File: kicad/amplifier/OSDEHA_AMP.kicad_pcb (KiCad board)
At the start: 2 copper layers, 190.1 x 71.6 mm, 85 parts, among them J1 INPUT, J2 HEATERS DC, J3 PSU HV, J4 OUTPUT, J5 DHT FIL, Q1 DN2540, Q10 DN2540, Q2 DN2540, Q3 STF3LN80K5, Q4 STF3LN80K5, Q5 AOT1N60, Q6 IXTP3N100D2, Q7 AOT1N60, Q8 IXTP3N100D2, Q9 DN2540, SW1 SW_DPDT_x2, U1 6E5P, U2 6E5P, U3 801A, U4 801A

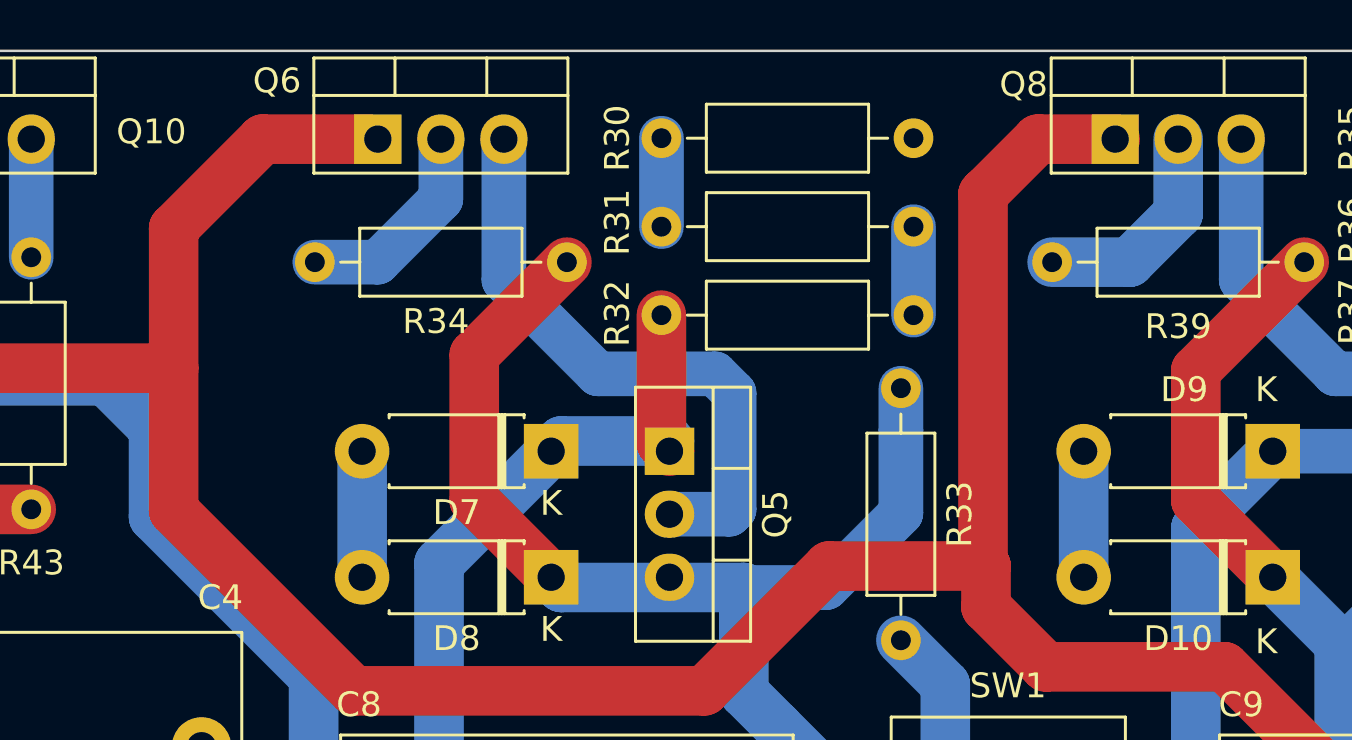
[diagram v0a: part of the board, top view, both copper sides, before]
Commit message: fixed pinout of Q6 and Q8 on PCB
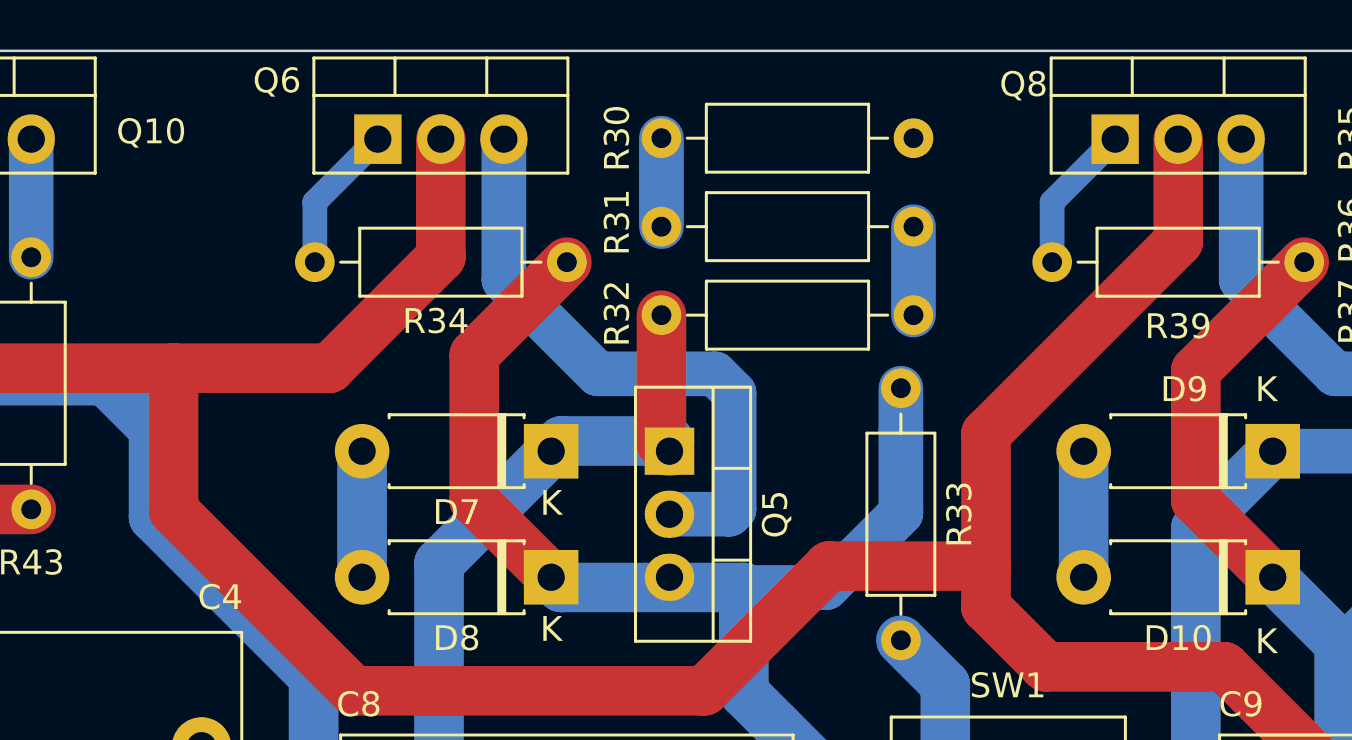
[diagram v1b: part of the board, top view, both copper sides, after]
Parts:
- R15, R20: value 25k -> 18.7k
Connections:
- Q6 pad 1: /B+ -> Net-(Q6-G)
- Q6 pad 2: Net-(Q6-G) -> /B+
- Q8 pad 1: /B+ -> Net-(Q8-G)
- Q8 pad 2: Net-(Q8-G) -> /B+
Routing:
- net Net-(Q8-G): track 9.02 -> 6.01 mm
- net Net-(Q6-G): track 8.55 -> 6.01 mm
- net /B+: track 256.2 -> 257.9 mm
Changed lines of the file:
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@@
 			)
 		)
+		(property ki_fp_filters "TO?220*")
 		(sheetname "Dual_Gyrator")
 		(sheetfile "Gyrator.kicad_sch")
@@
 			(layers "*.Cu" "*.Mask")
 			(remove_unused_layers no)
-			(net 17 "/B+")
-			(pinfunction "D")
-			(pintype "passive")
+			(net 27 "Net-(Q8-G)")
+			(pinfunction "G")
+			(pintype "input")
 		)
 		(pad "2" thru_hole oval
@@
 			(layers "*.Cu" "*.Mask")
 			(remove_unused_layers no)
-			(net 27 "Net-(Q8-G)")
-			(pinfunction "G")
-			(pintype "input")
+			(net 17 "/B+")
+			(pinfunction "D")
+			(pintype "passive")
 		)
 		(pad "3" thru_hole oval
@@
 			)
 		)
-		(property "Value" "25k"
+		(property "Value" "18.7k"
 			(at 5.08 2.37 90)
 			(layer "F.Fab")
@@
 			)
 		)
-		(property "MPN" "CMF5525K000"
+		(property "MPN" "CMF5520K000"
 			(at 0 0 0)
 			(layer "F.Fab")
@@
 			)
 		)
+		(property ki_fp_filters "TO?220*")
 		(sheetname "Dual_Gyrator")
 		(sheetfile "Gyrator.kicad_sch")
@@
 			(layers "*.Cu" "*.Mask")
 			(remove_unused_layers no)
-			(net 17 "/B+")
-			(pinfunction "D")
-			(pintype "passive")
+			(net 25 "Net-(Q6-G)")
+			(pinfunction "G")
+			(pintype "input")
 		)
 		(pad "2" thru_hole oval
@@
 			(layers "*.Cu" "*.Mask")
 			(remove_unused_layers no)
-			(net 25 "Net-(Q6-G)")
-			(pinfunction "G")
-			(pintype "input")
+			(net 17 "/B+")
+			(pinfunction "D")
+			(pintype "passive")
 		)
 		(pad "3" thru_hole oval
@@
 			(pintype "passive")
 		)
-		(model "${KICAD6_3DMODEL_DIR}/Package_TO_SOT_THT.3dshapes/TO-220-3_Vertical.wrl"
+		(model "${KICAD8_3DMODEL_DIR}/Package_TO_SOT_THT.3dshapes/TO-220-3_Vertical.wrl"
 			(offset
 				(xyz 0 0 0)
@@
 			)
 		)
-		(property "Value" "25k"
+		(property "Value" "18.7k"
 			(at 5.08 2.37 90)
 			(layer "F.Fab")
@@
 			)
 		)
-		(property "MPN" "CMF5525K000"
+		(property "MPN" "CMF5520K000"
 			(at 0 0 0)
 			(layer "F.Fab")
@@
 	)
 	(segment
-		(start 192.4304 56.7436)
-		(end 196.024 53.15)
+		(start 225.171 65.029)
+		(end 225.171 70.358)
+		(width 2)
+		(layer "F.Cu")
+		(net 17)
+	)
+	(segment
+		(start 198.7176 62.3824)
+		(end 192.4304 62.3824)
 		(width 2)
 		(layer "F.Cu")
@@
 	)
 	(segment
-		(start 196.024 53.15)
-		(end 200.2475 53.15)
-		(width 2)
-		(layer "F.Cu")
-		(net 17)
-	)
-	(segment
-		(start 225.05 70.237)
-		(end 225.171 70.358)
-		(width 2)
-		(layer "F.Cu")
-		(net 17)
-	)
-	(segment
-		(start 225.171 55.245)
-		(end 227.266 53.15)
+		(start 192.4304 62.3824)
+		(end 192.4304 68.1228)
 		(width 2)
 		(layer "F.Cu")
@@
 	)
 	(segment
-		(start 225.05 55.366)
-		(end 225.171 55.245)
+		(start 203.2 53.15)
+		(end 203.2 57.9)
 		(width 2)
 		(layer "F.Cu")
@@
 	)
 	(segment
-		(start 225.05 70.237)
-		(end 225.05 55.366)
+		(start 203.2 57.9)
+		(end 198.7176 62.3824)
 		(width 2)
 		(layer "F.Cu")
@@
 	)
 	(segment
-		(start 227.266 53.15)
-		(end 230.378 53.15)
+		(start 232.918 57.282)
+		(end 225.171 65.029)
 		(width 2)
 		(layer "F.Cu")
@@
 	)
 	(segment
-		(start 225.171 70.358)
-		(end 225.171 72.009)
+		(start 232.918 53.15)
+		(end 232.918 57.282)
 		(width 2)
 		(layer "F.Cu")
@@
 	)
 	(segment
-		(start 192.4304 56.7436)
-		(end 192.4304 68.1228)
+		(start 225.171 70.358)
+		(end 225.171 72.009)
 		(width 2)
 		(layer "F.Cu")
@@
 	)
 	(segment
+		(start 232.918 53.15)
+		(end 233.0055 53.2375)
+		(width 1)
+		(layer "B.Cu")
+		(net 17)
+	)
+	(segment
 		(start 87.5792 55.88)
 		(end 84.7142 53.015)
@@
 	)
 	(segment
-		(start 203.2 55.5625)
-		(end 200.6525 58.11)
-		(width 1.8)
-		(layer "B.Cu")
-		(net 25)
-	)
-	(segment
-		(start 200.6525 58.11)
-		(end 198.12 58.11)
-		(width 1.8)
+		(start 198.12 58.11)
+		(end 198.12 55.69)
+		(width 1)
 		(layer "B.Cu")
 		(net 25)
 	)
 	(segment
-		(start 203.2 53.15)
-		(end 203.2 55.5625)
-		(width 1.8)
+		(start 198.12 55.69)
+		(end 200.66 53.15)
+		(width 1)
 		(layer "B.Cu")
 		(net 25)
@@
 	)
 	(segment
-		(start 230.958 58.11)
-		(end 232.918 56.15)
-		(width 2)
+		(start 227.838 55.69)
+		(end 230.378 53.15)
+		(width 1)
 		(layer "B.Cu")
 		(net 27)
@@
 	(segment
 		(start 227.838 58.11)
-		(end 230.958 58.11)
-		(width 2)
-		(layer "B.Cu")
-		(net 27)
-	)
-	(segment
-		(start 232.918 56.15)
-		(end 232.918 53.15)
-		(width 2)
-		(layer "B.Cu")
-		(net 27)
-	)
-	(segment
-		(start 232.918 53.15)
-		(end 233.0055 53.2375)
+		(end 227.838 55.69)
 		(width 1)
 		(layer "B.Cu")

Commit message: changed R13 and R18 from 1M to 100k in schematic and PCB
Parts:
- R13, R18: value 1M -> 100k
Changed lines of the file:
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@@
 			)
 		)
-		(property "Value" "1M"
+		(property "Value" "100k"
 			(at 5.08 2.37 0)
 			(layer "F.Fab")
@@
 			)
 		)
-		(property "Value" "1M"
+		(property "Value" "100k"
 			(at 5.08 2.37 0)
 			(layer "F.Fab")

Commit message: revise R values in schematic and PCB files. Expand test/design notes.
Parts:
- R30, R31, R32, R35, R36, R37: value 1.5M -> 270k
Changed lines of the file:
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@@
 			)
 		)
-		(property "Value" "1.5M"
+		(property "Value" "270k"
 			(at 5.08 2.37 0)
 			(layer "F.Fab")
@@
 			)
 		)
-		(property "MPN" "CMF551M5000"
+		(property "MPN" "CMF55270K00"
 			(at 0 0 0)
 			(layer "F.Fab")
@@
 			)
 		)
-		(property "Value" "1.5M"
+		(property "Value" "270k"
 			(at 5.08 2.37 0)
 			(layer "F.Fab")
@@
 			)
 		)
-		(property "MPN" "CMF551M5000"
+		(property "MPN" "CMF55270K00"
 			(at 0 0 0)
 			(layer "F.Fab")
@@
 			)
 		)
-		(property "MPN" "CMF551M000"
+		(property "MPN" "CMF55100K00"
 			(at 0 0 0)
 			(layer "F.Fab")
@@
 			)
 		)
-		(property "Value" "1.5M"
+		(property "Value" "270k"
 			(at 5.08 2.37 0)
 			(layer "F.Fab")
@@
 			)
 		)
-		(property "MPN" "CMF551M5000"
+		(property "MPN" "CMF55270K00"
 			(at 0 0 0)
 			(layer "F.Fab")
@@
 			)
 		)
-		(property "Value" "1.5M"
+		(property "Value" "270k"
 			(at 5.08 2.37 0)
 			(layer "F.Fab")
@@
 			)
 		)
-		(property "MPN" "CMF551M5000"
+		(property "MPN" "CMF55270K00"
 			(at 0 0 0)
 			(layer "F.Fab")
@@
 			)
 		)
-		(property "Value" "1.5M"
+		(property "Value" "270k"
 			(at 5.08 2.37 0)
 			(layer "F.Fab")
@@
 			)
 		)
-		(property "MPN" "CMF551M5000"
+		(property "MPN" "CMF55270K00"
 			(at 0 0 0)
 			(layer "F.Fab")
@@
 			)
 		)
-		(property "MPN" "CMF551M0000"
+		(property "MPN" "CMF55100K00"
 			(at 0 0 0)
 			(layer "F.Fab")
@@
 			)
 		)
-		(property "Value" "1.5M"
+		(property "Value" "270k"
 			(at 5.08 2.37 0)
 			(layer "F.Fab")
@@
 			)
 		)
-		(property "MPN" "CMF551M5000"
+		(property "MPN" "CMF55270K00"
 			(at 0 0 0)
 			(layer "F.Fab")

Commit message: notes, design tweaks
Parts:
- R33, R38: footprint Resistor_THT:R_Axial_DIN0207_L6.3mm_D2.5mm_P10.16mm_Horizontal -> Resistor_THT:R_Axial_DIN0516_L15.5mm_D5.0mm_P5.08mm_Vertical
- moved R33 6.99 mm to (220.2, 70.0), turned to 90 degrees
- moved R38 6.76 mm to (251.2, 70.0), turned to 90 degrees
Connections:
- R33 pad 1: /Dual_Gyrator/MU_OUT1 -> /A1
- R33 pad 2: /A1 -> /Dual_Gyrator/MU_OUT1
- R38 pad 1: /Dual_Gyrator/MU_OUT2 -> /A2
- R38 pad 2: /A2 -> /Dual_Gyrator/MU_OUT2
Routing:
- net /A1: track 74.6 -> 79.0 mm
- net /Dual_Gyrator/MU_OUT1: track 53.9 -> 49.6 mm
- net /A2: track 129.1 -> 132.5 mm
- net /Dual_Gyrator/MU_OUT2: track 61.2 -> 58.3 mm
- net /B+: track 257.9 -> 260.2 mm

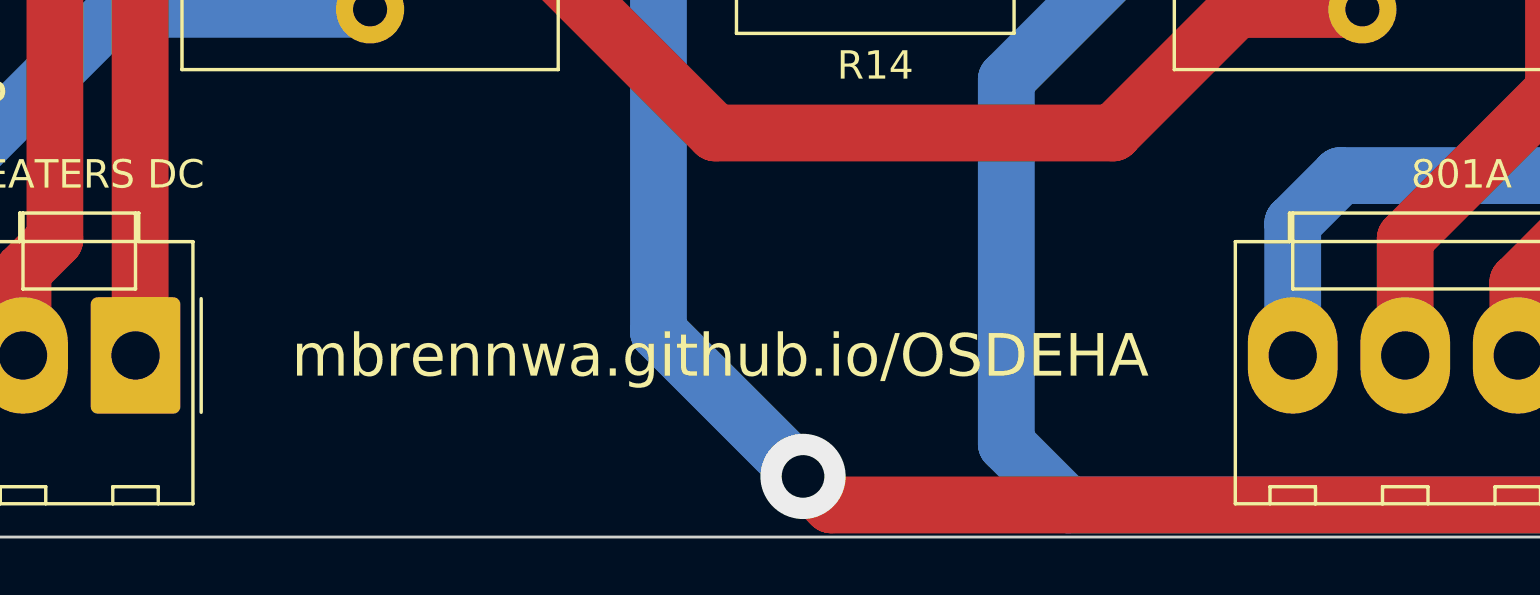
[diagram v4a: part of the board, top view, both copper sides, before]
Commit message: add version info to silk screens (AMP + HV PSU)
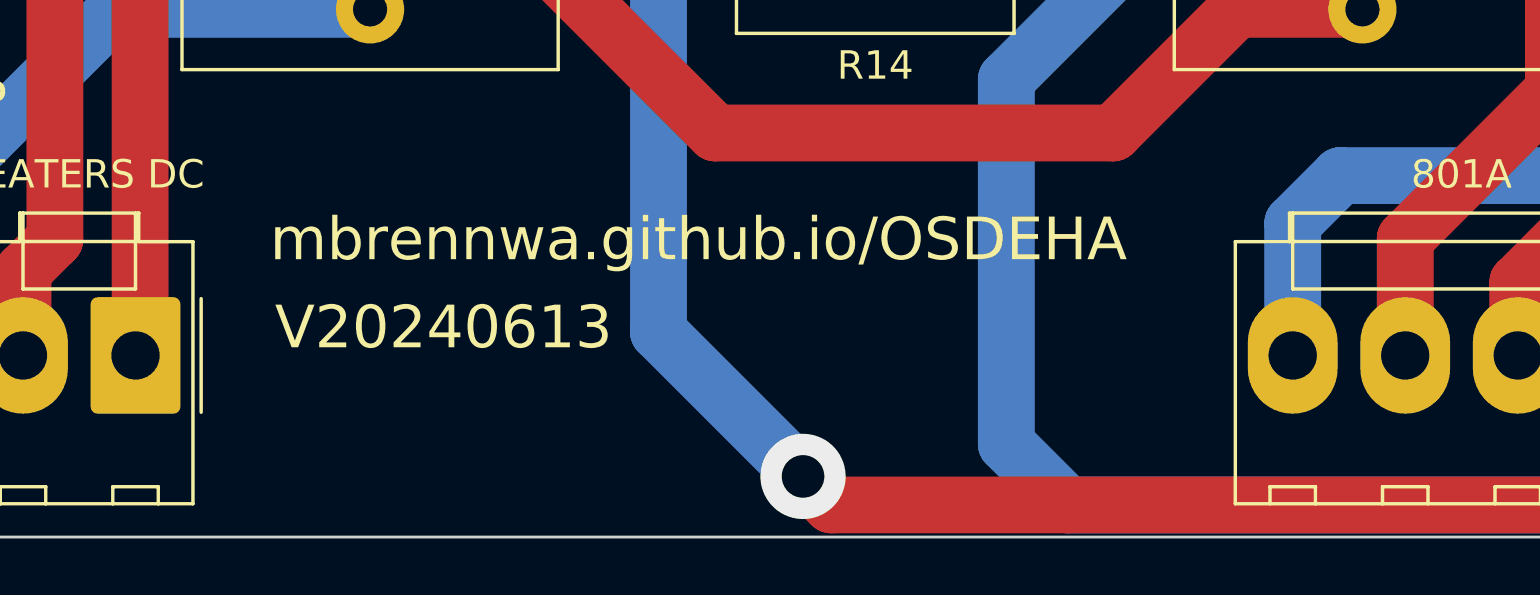
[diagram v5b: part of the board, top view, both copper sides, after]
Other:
- board text added: "V20240613"
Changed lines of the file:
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@@
 		(tags "Resistor Axial_DIN0516 series Axial Vertical pin pitch 5.08mm 2W length 15.5mm diameter 5mm")
 		(property "Reference" "R38"
-			(at 4.6 2.605 270)
+			(at 4.6 2.605 -90)
 			(layer "F.SilkS")
 			(effects
@@
 		)
 		(property "Value" "470"
-			(at 2.54 3.62 270)
+			(at 2.54 3.62 -90)
 			(layer "F.Fab")
 			(hide yes)
@@
 		)
 		(fp_text user "${REFERENCE}"
-			(at 2.54 -3.62 270)
+			(at 2.54 -3.62 -90)
 			(layer "F.Fab")
 			(effects
@@
 		(tags "Resistor Axial_DIN0516 series Axial Vertical pin pitch 5.08mm 2W length 15.5mm diameter 5mm")
 		(property "Reference" "R33"
-			(at 4.59 2.8 270)
+			(at 4.59 2.8 -90)
 			(layer "F.SilkS")
 			(effects
@@
 		)
 		(property "Value" "470"
-			(at 2.54 3.62 270)
+			(at 2.54 3.62 -90)
 			(layer "F.Fab")
 			(hide yes)
@@
 		)
 		(property "MPN" " CPF3470R00"
-			(at 0 0 360)
+			(at 0 0 0)
 			(layer "F.Fab")
 			(hide yes)
@@
 		)
 		(fp_text user "${REFERENCE}"
-			(at 2.54 -3.62 270)
+			(at 2.54 -3.62 -90)
 			(layer "F.Fab")
 			(effects
@@
 		(layer "Edge.Cuts")
 	)
+	(gr_text "V20240613"
+		(at 130 114.725 0)
+		(layer "F.SilkS")
+		(effects
+			(font
+				(size 1.5 1.5)
+				(thickness 0.15)
+			)
+			(justify left bottom)
+		)
+	)
 	(gr_text "mbrennwa.github.io/OSDEHA"
-		(at 145.675 115.725 0)
+		(at 129.825 111.625 0)
 		(layer "F.SilkS")
 		(effects
@@
 				(thickness 0.15)
 			)
-			(justify bottom)
+			(justify left bottom)
 		)
 	)

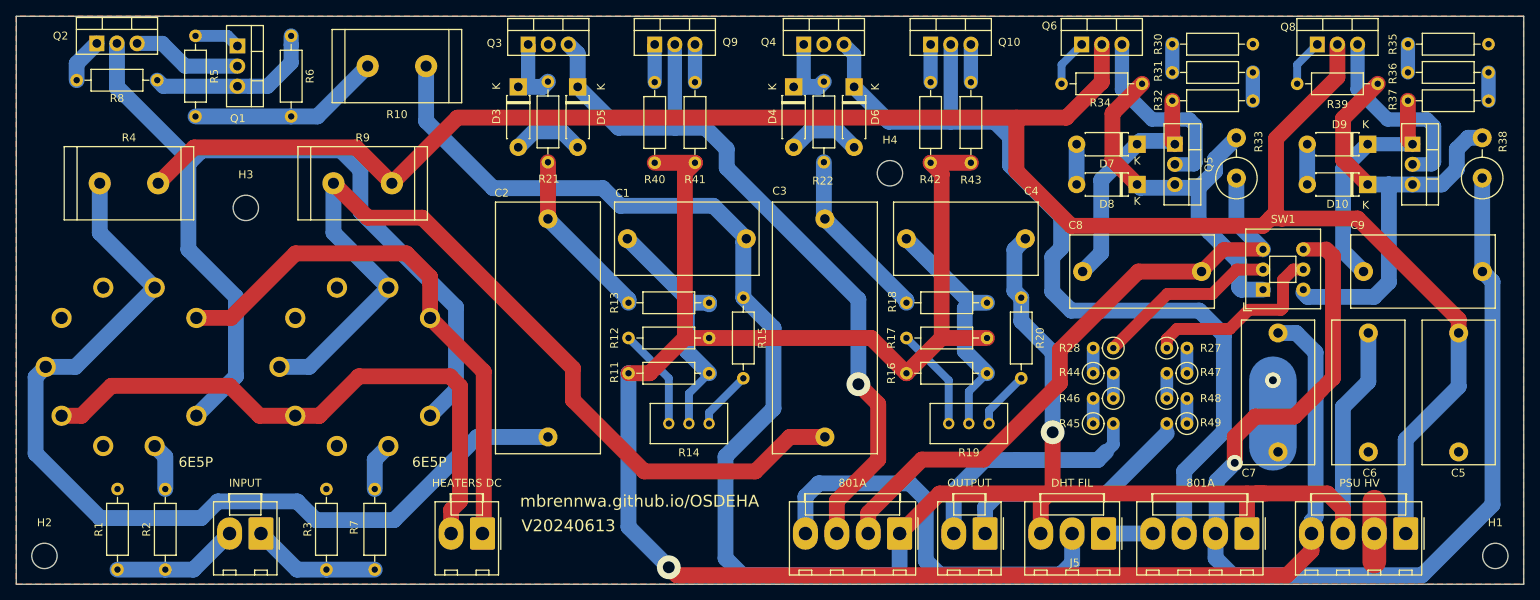
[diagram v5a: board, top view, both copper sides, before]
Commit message: add gate stopper for CCS FET in output stage / mu follower
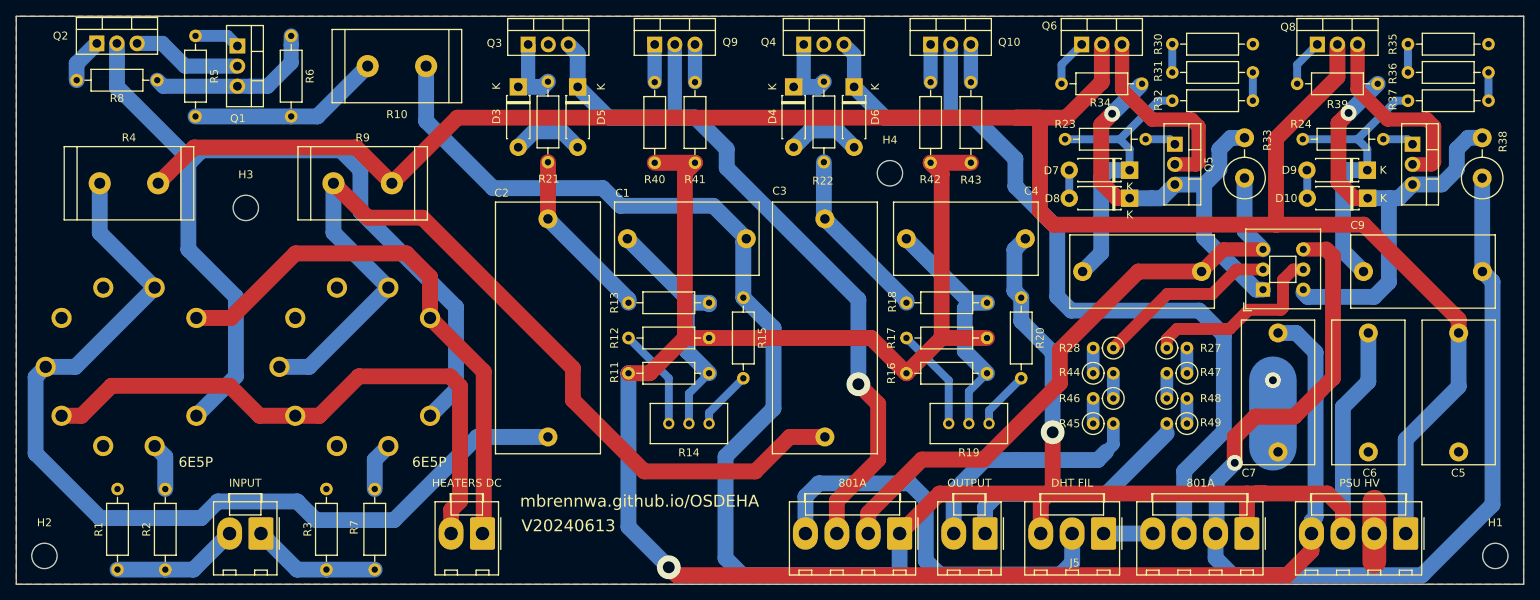
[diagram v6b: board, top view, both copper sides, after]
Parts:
- added R23: 330, Resistor_THT:R_Axial_DIN0207_L6.3mm_D2.5mm_P10.16mm_Horizontal, F.Cu at (208.7, 65.1)
- added R24: 330, Resistor_THT:R_Axial_DIN0207_L6.3mm_D2.5mm_P10.16mm_Horizontal, F.Cu at (238.7, 65.1)
- moved D7 3.40 mm to (206.7, 69.0)
- moved D9 3.27 mm to (236.7, 69.0)
- moved D8 1.96 mm to (206.7, 72.5)
- moved D10 1.72 mm to (236.7, 72.5)
- moved R33 1.02 mm to (221.2, 70.0)
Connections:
- Q5 pad 1: Net-(D7-K) -> Net-(Q5-G)
- Q7 pad 1: Net-(D9-K) -> Net-(Q7-G)
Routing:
- net Net-(D9-K): track 29.1 -> 36.6 mm
- net Net-(D7-K): track 29.5 -> 36.5 mm
- net /Dual_Gyrator/MU_OUT1: track 49.6 -> 54.7 mm, vias 0 -> 1
- net Net-(Q7-G): track 0.00 -> 4.53 mm
- net Net-(Q5-G): track 0.00 -> 3.95 mm
- net /G2: track 111.5 -> 108.9 mm
- net /Dual_Gyrator/MU_OUT2: track 58.3 -> 60.5 mm, vias 0 -> 1
- net /B+: track 260.2 -> 261.8 mm
- net Net-(D7-A): track 5.08 -> 3.53 mm
- net Net-(D10-A): track 5.08 -> 3.55 mm
